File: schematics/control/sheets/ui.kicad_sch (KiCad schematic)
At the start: 11 parts

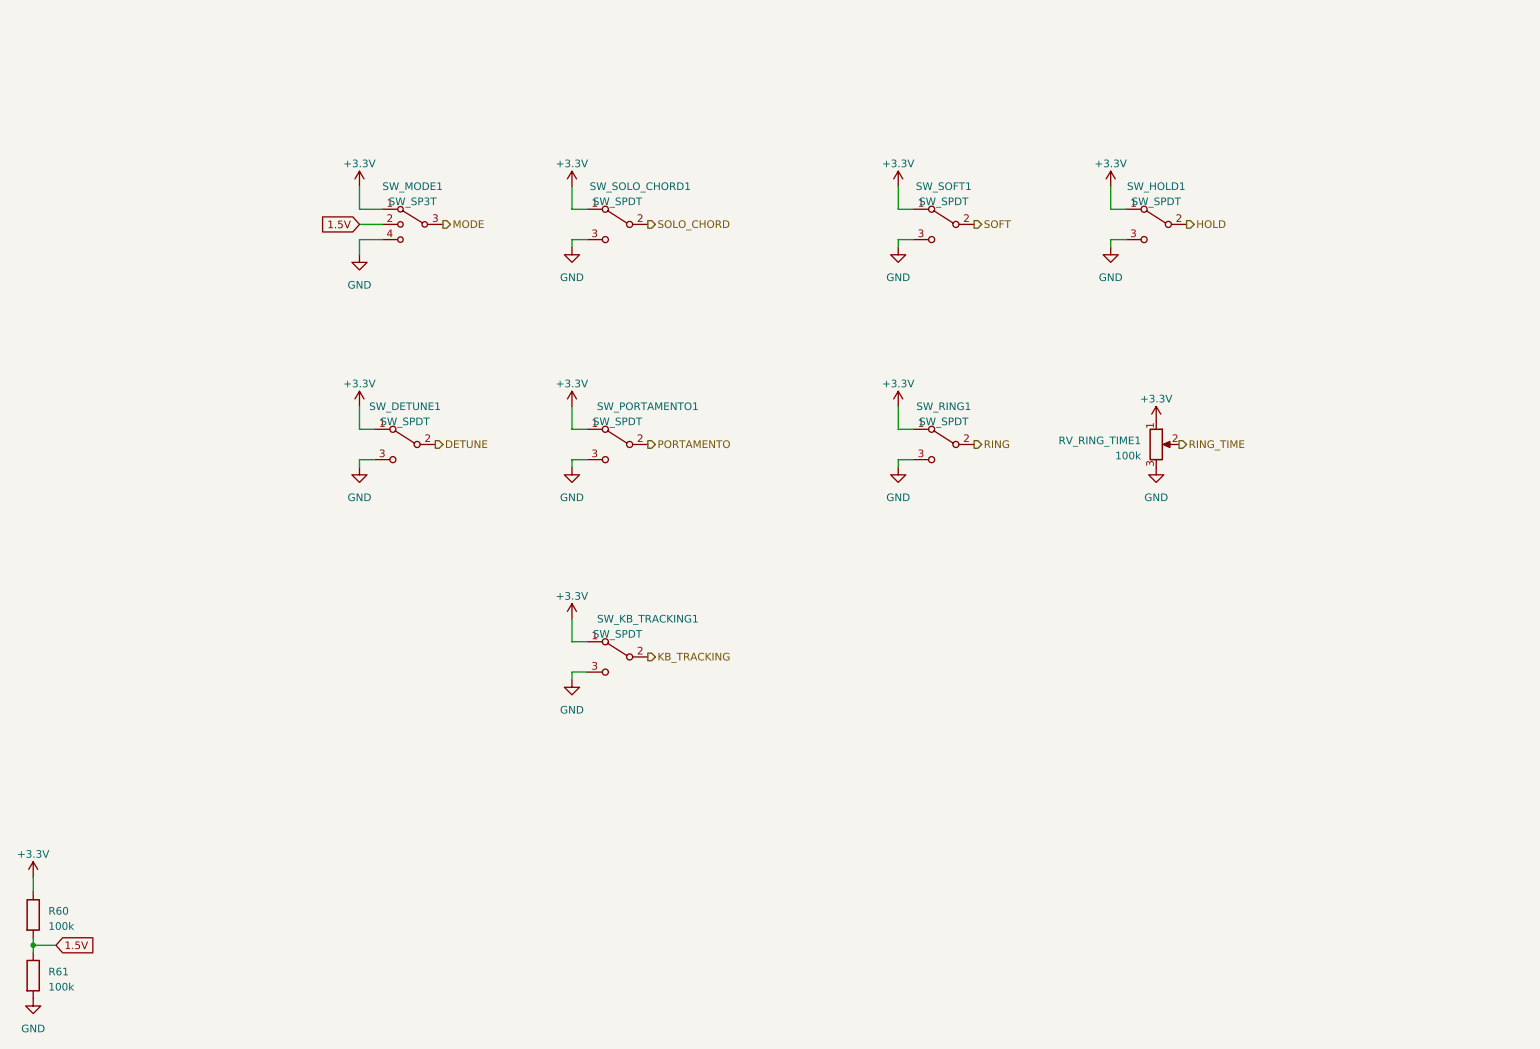
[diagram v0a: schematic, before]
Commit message: Updated MUX reading
For some reason I couldn't figure out yet, there was one step offset
in the reading of the multiplexer input. :/ Now it works as intended
but it's still annoying.
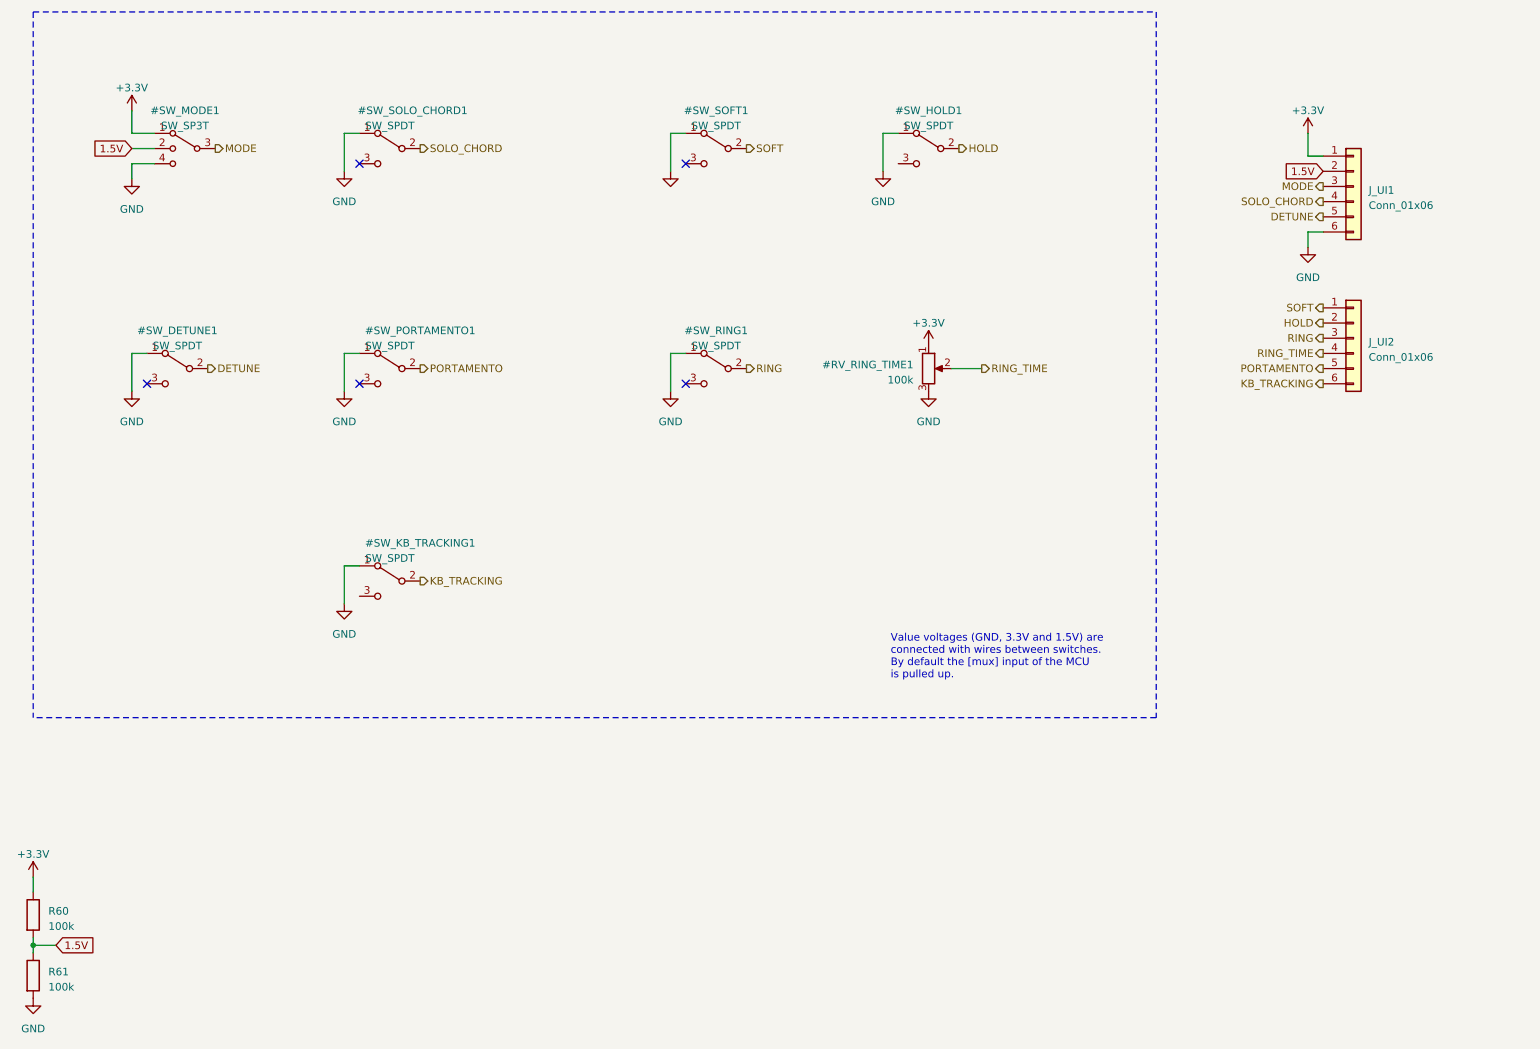
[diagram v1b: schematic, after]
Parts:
- added J_UI1, J_UI2: Conn_01x06, symbol Connector_Generic:Conn_01x06
- renumbered RV_RING_TIME1 to #RV_RING_TIME1, SW_DETUNE1 to #SW_DETUNE1, SW_HOLD1 to #SW_HOLD1, SW_KB_TRACKING1 to #SW_KB_TRACKING1, SW_MODE1 to #SW_MODE1, SW_PORTAMENTO1 to #SW_PORTAMENTO1, SW_RING1 to #SW_RING1, SW_SOFT1 to #SW_SOFT1, SW_SOLO_CHORD1 to #SW_SOLO_CHORD1
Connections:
- net +3.3V: now also J_UI1.1 (Pin_1); no longer #SW_DETUNE1.1 (A), #SW_HOLD1.1 (A), #SW_KB_TRACKING1.1 (A), #SW_PORTAMENTO1.1 (A), #SW_RING1.1 (A), #SW_SOFT1.1 (A), #SW_SOLO_CHORD1.1 (A)
- net 1.5V: now also J_UI1.2 (Pin_2)
- net DETUNE: now also J_UI1.5 (Pin_5)
- net GND: now also #SW_DETUNE1.1 (A), #SW_HOLD1.1 (A), #SW_KB_TRACKING1.1 (A), #SW_PORTAMENTO1.1 (A), #SW_RING1.1 (A), #SW_SOFT1.1 (A), #SW_SOLO_CHORD1.1 (A), J_UI1.6 (Pin_6); no longer #SW_DETUNE1.3 (C), #SW_HOLD1.3 (C), #SW_KB_TRACKING1.3 (C), #SW_PORTAMENTO1.3 (C), #SW_RING1.3 (C), #SW_SOFT1.3 (C), #SW_SOLO_CHORD1.3 (C)
- net HOLD: now also J_UI2.2 (Pin_2)
- net KB_TRACKING: now also J_UI2.6 (Pin_6)
- net MODE: now also J_UI1.3 (Pin_3)
- net PORTAMENTO: now also J_UI2.5 (Pin_5)
- net RING: now also J_UI2.3 (Pin_3)
- net RING_TIME: now also J_UI2.4 (Pin_4)
- net SOFT: now also J_UI2.1 (Pin_1)
- net SOLO_CHORD: now also J_UI1.4 (Pin_4)
- no-connect marks 0 -> 5
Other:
- note added: "Value voltages (GND, 3.3V and 1.5V) are connected with wires between switches. By default the [mux] input of the MCU is pulled up."

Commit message: Schemo work
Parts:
- added J_UI3: Conn_01x02, Shmoergh_Custom_Footprints:NSL25_01x02_Vertical, symbol Connector_Generic:Conn_01x02
- J_UI1, J_UI2: footprint (none) -> Shmoergh_Custom_Footprints:NSL25_01x06_Vertical
- R60, R61: footprint (none) -> Shmoergh_Custom_Footprints:R_Axial_DIN0207_L6.3mm_D2.5mm_P7.62mm_Horizontal
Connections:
- new net EXTRA_GPIO1: J_UI3.1 (Pin_1)
- new net EXTRA_GPIO2: J_UI3.2 (Pin_2)
- no-connect marks 5 -> 7
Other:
- note added: "These could be NTF connectors, or ribbon cables too. Maybe it's better to add both?"
